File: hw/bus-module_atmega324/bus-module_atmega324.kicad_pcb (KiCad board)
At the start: 2 copper layers, 35 x 48 mm, 35 parts, among them J1 CONN_10X2, J2 CONN_10X2, J3 CONN-ISP-6, J5 CONN_1, J6 CONN_1, J7 CONN_1, J8 CONN_1, U1 ATMEGA324-TQFP44, U2 7,3728MHz, U3 25LCXXX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

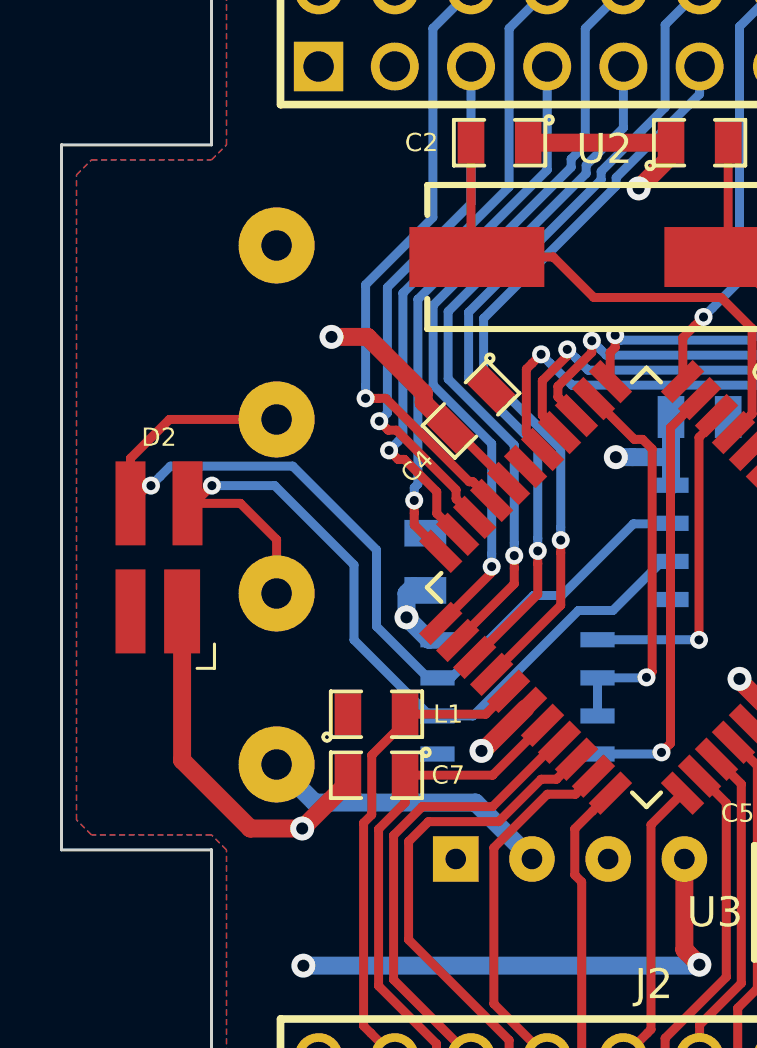
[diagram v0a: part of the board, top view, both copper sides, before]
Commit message: Start of development of Rev. B: - integrated fuse for 24V supply. - new footprint SOT143 for TVS-Diode. - replaced TVS-Diode footprint by SOT143. - added revision text on copper layer.
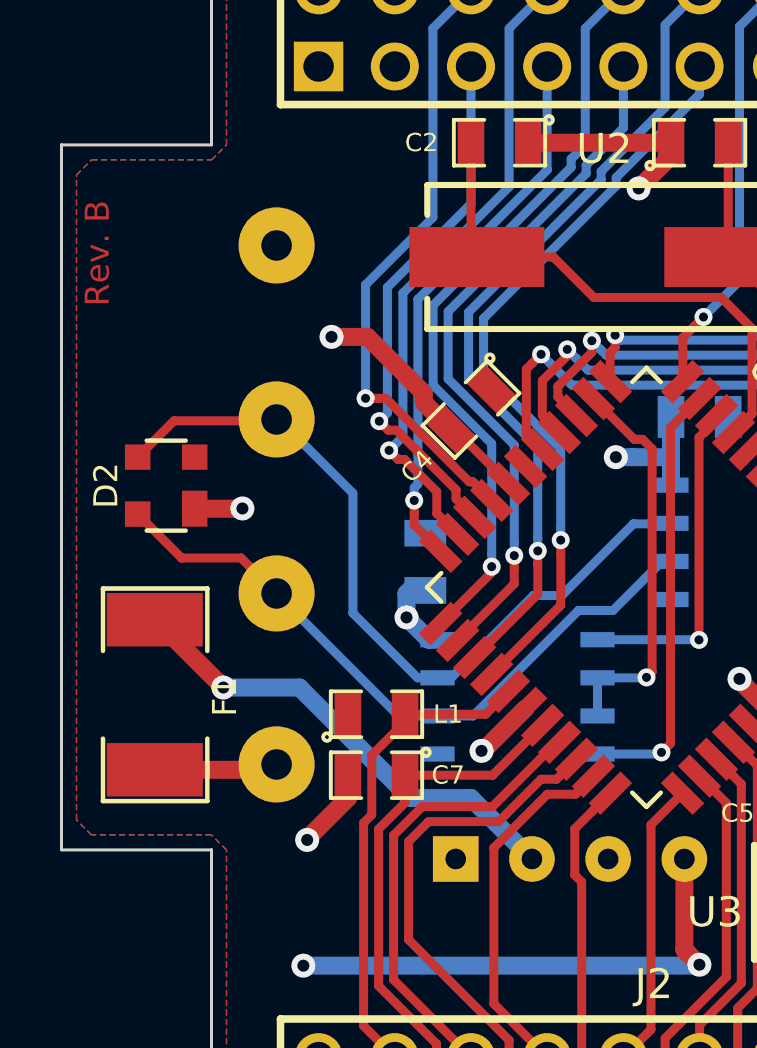
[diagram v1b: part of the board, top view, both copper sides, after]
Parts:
- added F1: FUSE, Resistor:R_1812, F.Cu at (83.1, 104.3)
- D2: footprint Housings_SOT:SOT143R_Diode_Reverse -> Diode_SMD:SOT143
- moved D2 2.40 mm to (83.5, 97.4), turned to 90 degrees
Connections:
- J5 pad 1: +24V -> Net-(F1-Pad2)
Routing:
- net GND: track 56.4 -> 49.0 mm, vias 7 -> 8
- net /A: track 29.4 -> 23.1 mm, vias 1 -> 0
- net +24V: track 9.82 -> 15.9 mm, vias 0 -> 1
- net /B: track 32.5 -> 26.7 mm, vias 1 -> 0
- net Net-(F1-Pad2): track 0.00 -> 4.24 mm
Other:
- board text added: "Rev. B"

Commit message: SPI resistors changed from 1k to 100
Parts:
- R2, R3, R4: value 1k -> 100
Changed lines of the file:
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@@
-(kicad_pcb (version 4) (host pcbnew "(2015-09-05 BZR 6159)-product")
+(kicad_pcb (version 20170123) (host pcbnew no-vcs-found-7600~57~ubuntu14.04.1)
   (general
     (links 116)
     (no_connects 0)
-    (area 52.678572 64.65 172.77 131.450001)
+    (area 79.949999 75.947965 115.054227 124.050001)
     (thickness 1.6)
     (drawings 41)
@@
       (hpglpenspeed 20)
       (hpglpendiameter 15)
-      (hpglpenoverlay 2)
       (psnegative false)
       (psa4output false)
@@
     (tags "CMS SOJ")
     (attr smd)
-    (fp_text reference U4 (at -3.6 -2.8 360) (layer B.SilkS)
+    (fp_text reference U4 (at -3.6 -2.8) (layer B.SilkS)
       (effects (font (size 1 1) (thickness 0.15)) (justify mirror))
     )
@@
     (at 101.27 95.0715 180)
     (attr smd)
-    (fp_text reference C10 (at 0.65 1.5 360) (layer B.SilkS)
+    (fp_text reference C10 (at 0.65 1.5) (layer B.SilkS)
       (effects (font (size 0.6096 0.6096) (thickness 0.1016)) (justify mirror))
     )
@@
     (at 92.126 99.8975 270)
     (attr smd)
-    (fp_text reference C11 (at -0.95 -1.778 360) (layer B.SilkS)
+    (fp_text reference C11 (at -0.95 -1.778) (layer B.SilkS)
       (effects (font (size 0.6096 0.6096) (thickness 0.1016)) (justify mirror))
     )
@@
       (effects (font (size 0.6096 0.6096) (thickness 0.1016)))
     )
-    (fp_text value 1k (at 0 0 45) (layer F.SilkS) hide
+    (fp_text value 100 (at 0 0 45) (layer F.SilkS) hide
       (effects (font (size 0.6096 0.6096) (thickness 0.1016)))
     )
@@
       (effects (font (size 0.6096 0.6096) (thickness 0.1016)))
     )
-    (fp_text value 1k (at 0 0 45) (layer F.SilkS) hide
+    (fp_text value 100 (at 0 0 45) (layer F.SilkS) hide
       (effects (font (size 0.6096 0.6096) (thickness 0.1016)))
     )
@@
       (effects (font (size 0.6096 0.6096) (thickness 0.1016)))
     )
-    (fp_text value 1k (at 0 0 45) (layer F.SilkS) hide
+    (fp_text value 100 (at 0 0 45) (layer F.SilkS) hide
       (effects (font (size 0.6096 0.6096) (thickness 0.1016)))
     )
@@
     (at 106.35 87.1975 270)
     (attr smd)
-    (fp_text reference R6 (at 0.508 1.524 360) (layer F.SilkS)
+    (fp_text reference R6 (at 0.508 1.524) (layer F.SilkS)
       (effects (font (size 0.6096 0.6096) (thickness 0.1016)))
     )
@@
     (tags "CMS SOJ")
     (attr smd)
-    (fp_text reference U5 (at -3.45 -3 360) (layer B.SilkS)
+    (fp_text reference U5 (at -3.45 -3) (layer B.SilkS)
       (effects (font (size 1 1) (thickness 0.15)) (justify mirror))
     )
@@
   (module Diode:SOD323 (layer F.Cu)
     (at 106.25 90.7535 270)
-    (fp_text reference D1 (at 0.762 1.424 360) (layer F.SilkS)
+    (fp_text reference D1 (at 0.762 1.424) (layer F.SilkS)
       (effects (font (size 0.6096 0.6096) (thickness 0.1016)))
     )
@@
     (tags "QFP 0.8")
     (attr smd)
-    (fp_text reference U1 (at -7.960962 1.865701 495) (layer F.SilkS)
+    (fp_text reference U1 (at -7.960962 1.865701 135) (layer F.SilkS)
       (effects (font (size 1 1) (thickness 0.15)))
     )
@@
       (effects (font (size 0.8 0.8) (thickness 0.15)))
     )
-    (fp_text value FUSE (at 0 0.0508 360) (layer F.Fab)
+    (fp_text value FUSE (at 0 0.0508) (layer F.Fab)
       (effects (font (size 0.8 0.8) (thickness 0.15)))
     )
